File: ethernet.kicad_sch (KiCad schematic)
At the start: 43 parts, among them J5 ARJM11D7-502-AB-EW2, U1 MIMX8MM6DVTLZAA, U23 RTL8211FD, U24 TPD4EUSB30, U25 TPD4EUSB30, Y2 25MHz

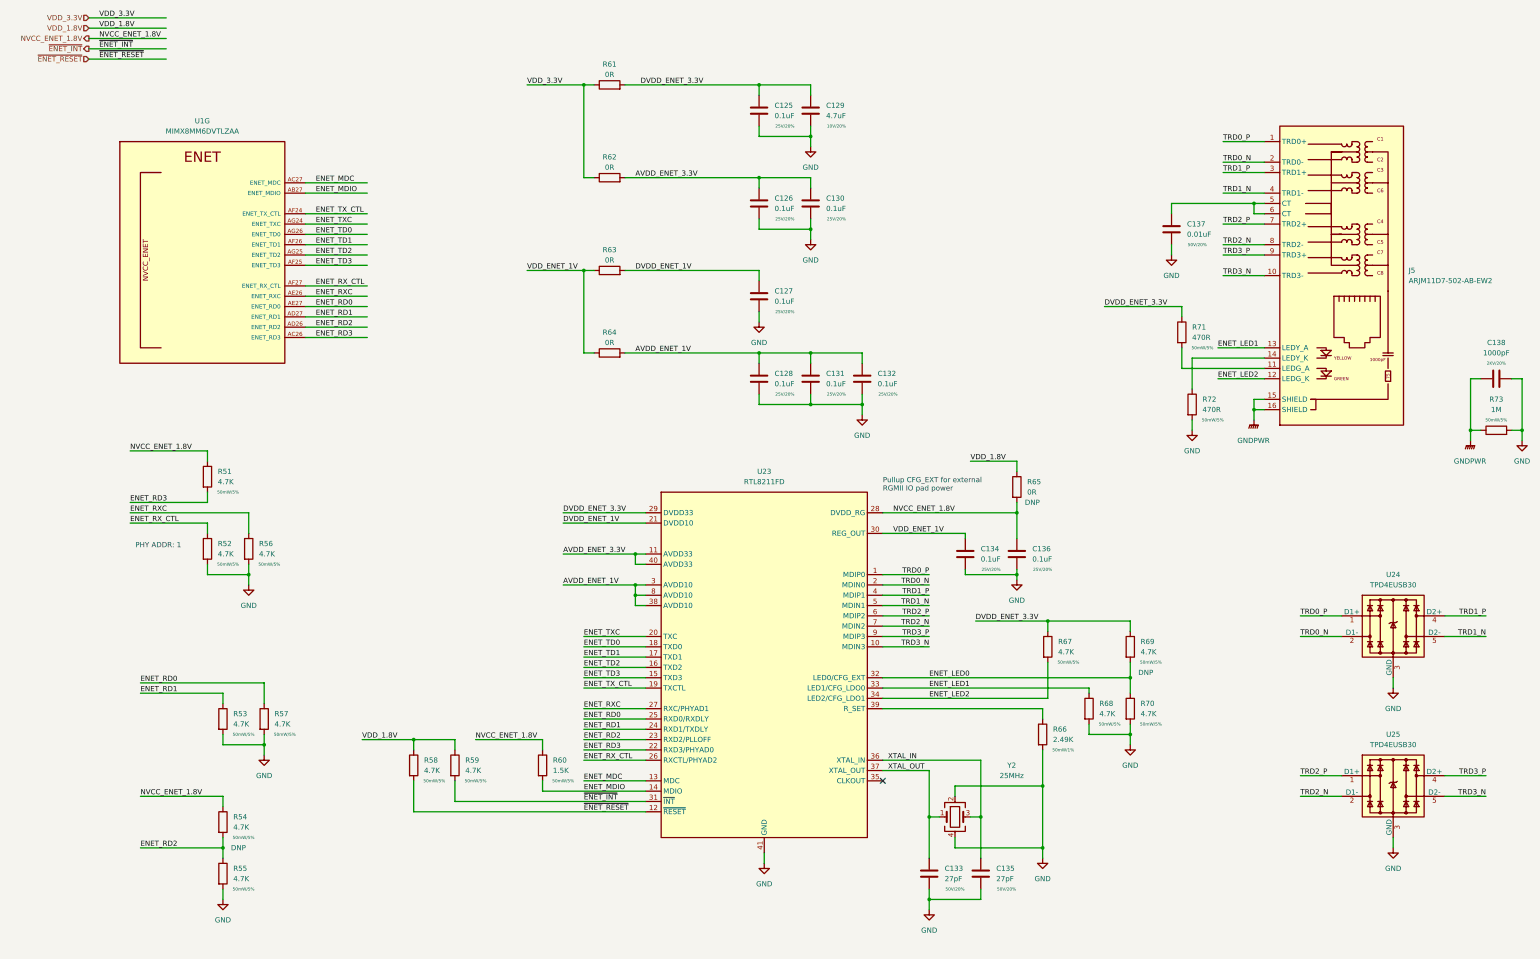
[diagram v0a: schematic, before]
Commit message: add inital ddr tool version, lots of routing work
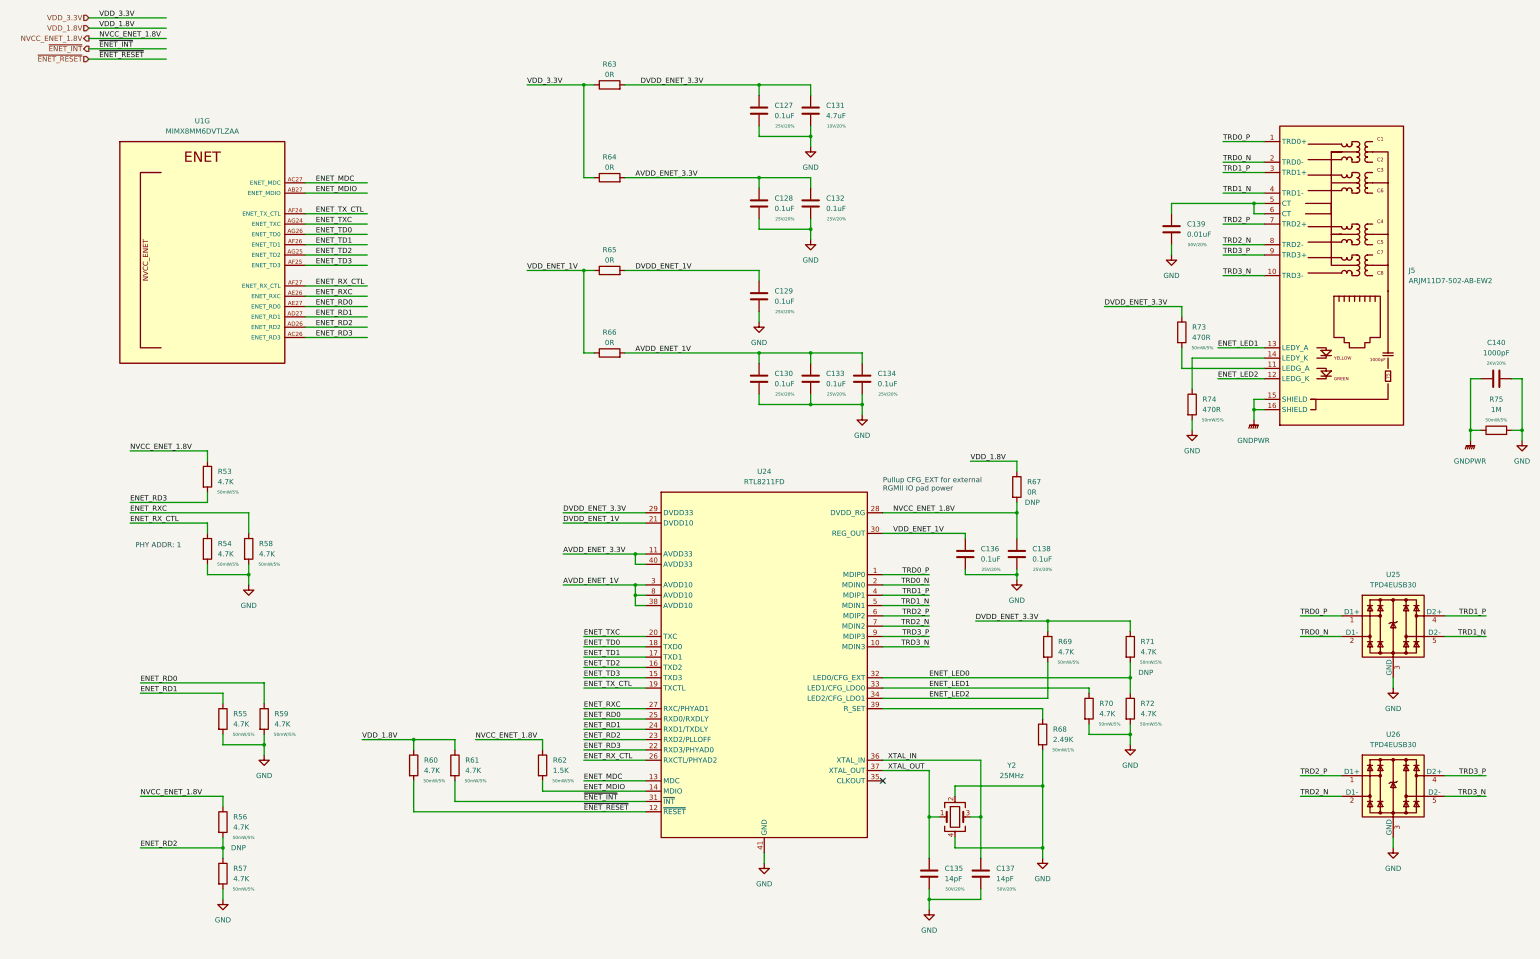
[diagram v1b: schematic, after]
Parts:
- C135: renamed from C133; value 27pF -> 14pF
- C137: renamed from C135; value 27pF -> 14pF
- Y2: MPN (none) -> ECS-250-10-33B-CWN-TR
- renumbered C125 to C127, C126 to C128, C127 to C129, C128 to C130, C129 to C131, C130 to C132, C131 to C133, C132 to C134, C134 to C136, C136 to C138, C137 to C139, C138 to C140, R51 to R53, R52 to R54, R53 to R55, R54 to R56, R55 to R57, R56 to R58, R57 to R59, R58 to R60, R59 to R61, R60 to R62, R61 to R63, R62 to R64, R63 to R65, R64 to R66, R65 to R67, R66 to R68, R67 to R69, R68 to R70, R69 to R71, R70 to R72, R71 to R73, R72 to R74, R73 to R75, U23 to U24, U24 to U25, U25 to U26

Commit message: v2 of ddr flytimes tool, lots of routing work, sch fixes
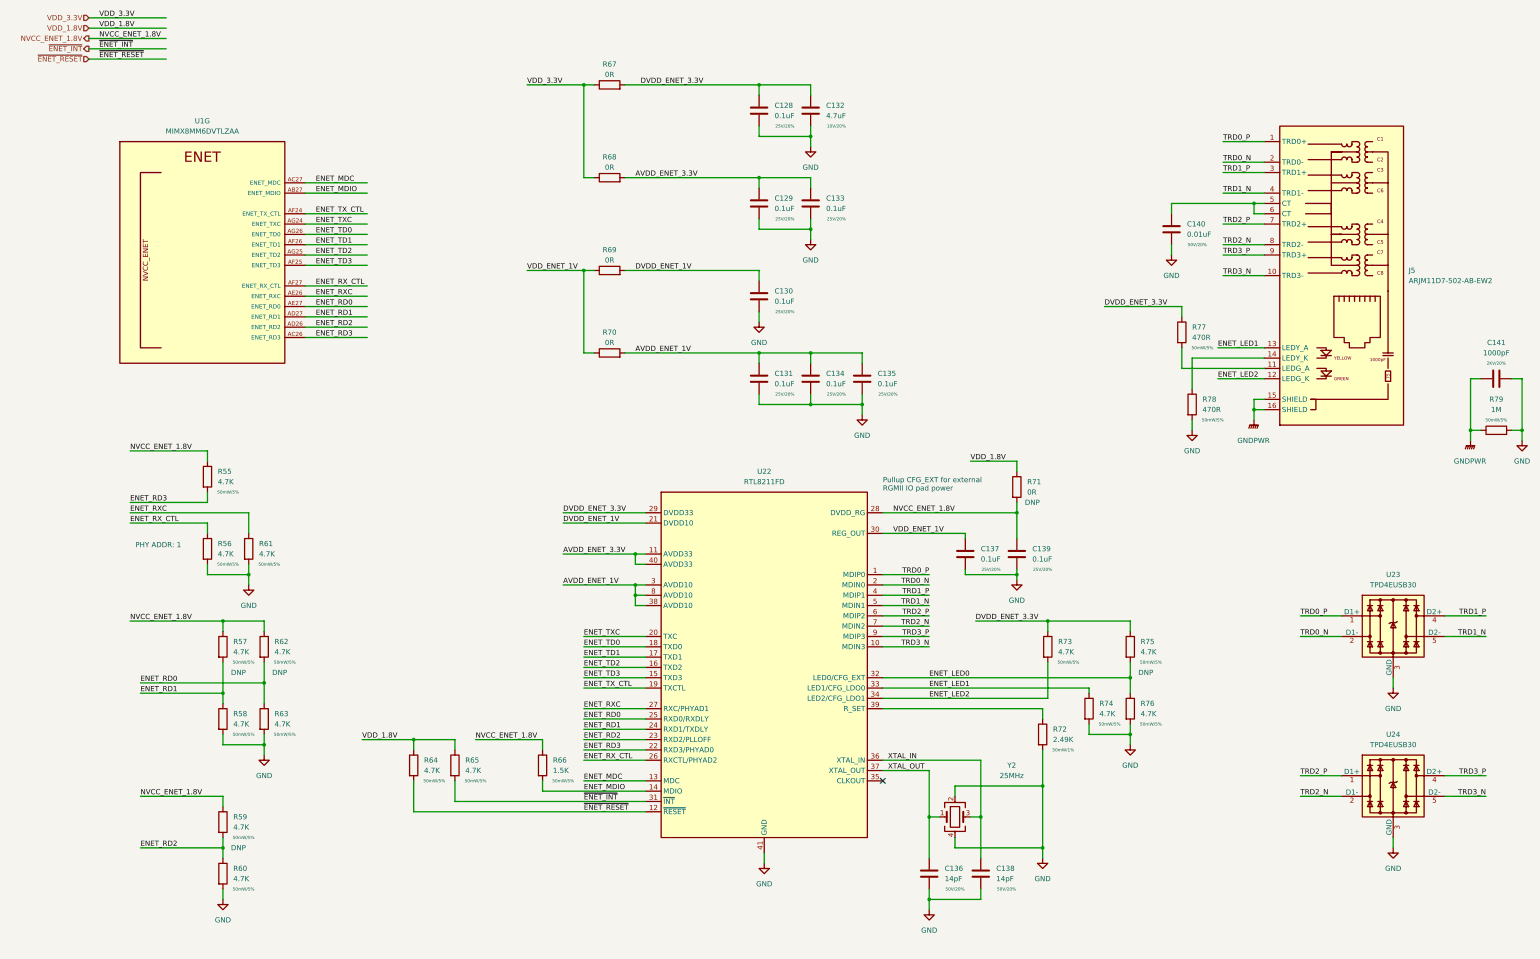
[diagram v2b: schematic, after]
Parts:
- added R57, R62: 4.7K, Resistor_SMD:R_0402_1005Metric, symbol Device:R
- renumbered C127 to C128, C128 to C129, C129 to C130, C130 to C131, C131 to C132, C132 to C133, C133 to C134, C134 to C135, C135 to C136, C136 to C137, C137 to C138, C138 to C139, C139 to C140, C140 to C141, R53 to R55, R54 to R56, R55 to R58, R56 to R59, R57 to R60, R58 to R61, R59 to R63, R60 to R64, R61 to R65, R62 to R66, R63 to R67, R64 to R68, R65 to R69, R66 to R70, R67 to R71, R68 to R72, R69 to R73, R70 to R74, R71 to R75, R72 to R76, R73 to R77, R74 to R78, R75 to R79, U24 to U22, U25 to U23, U26 to U24
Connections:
- net ENET_RD0: now also R62.2
- net ENET_RD1: now also R57.2
- net NVCC_ENET_1.8V: now also R57.1, R62.1

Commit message: more routing work, prepare to change to x32 lpddr4
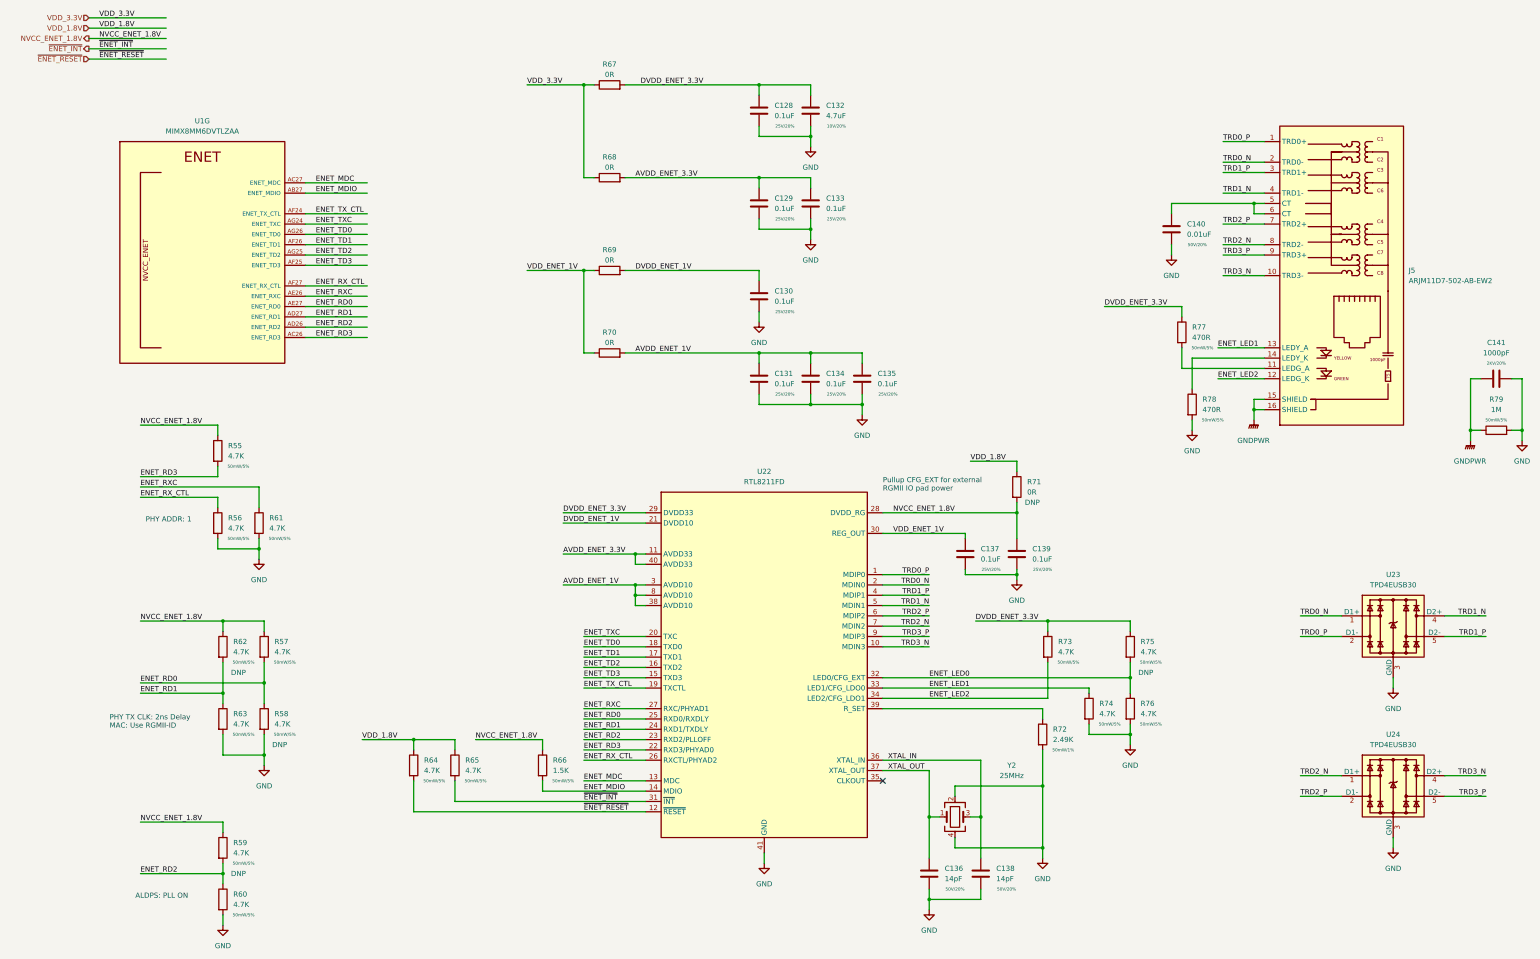
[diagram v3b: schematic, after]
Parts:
- R57: DNP DNP -> (none)
- R58: DNP (none) -> DNP
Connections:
- net ENET_RD0: now also R57.2, R58.1; no longer R62.2, R63.1
- net ENET_RD1: now also R62.2, R63.1; no longer R57.2, R58.1
- net TRD0_N: now also U23.1 (D1+), U23.10; no longer U23.2 (D1-), U23.9
- net TRD0_P: now also U23.2 (D1-), U23.9; no longer U23.1 (D1+), U23.10
- net TRD1_N: now also U23.4 (D2+), U23.7; no longer U23.5 (D2-), U23.6
- net TRD1_P: now also U23.5 (D2-), U23.6; no longer U23.4 (D2+), U23.7
- net TRD2_N: now also U24.1 (D1+), U24.10; no longer U24.2 (D1-), U24.9
- net TRD2_P: now also U24.2 (D1-), U24.9; no longer U24.1 (D1+), U24.10
- net TRD3_N: now also U24.4 (D2+), U24.7; no longer U24.5 (D2-), U24.6
- net TRD3_P: now also U24.5 (D2-), U24.6; no longer U24.4 (D2+), U24.7
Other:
- note added: "ALDPS: PLL ON"
- note added: "PHY TX CLK: 2ns Delay MAC: Use RGMII-ID"
- moved on the sheet: R55, R56, R57, R58, R59, R60, R61, R62, R63

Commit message: inital routing of ddr data bus, sch work
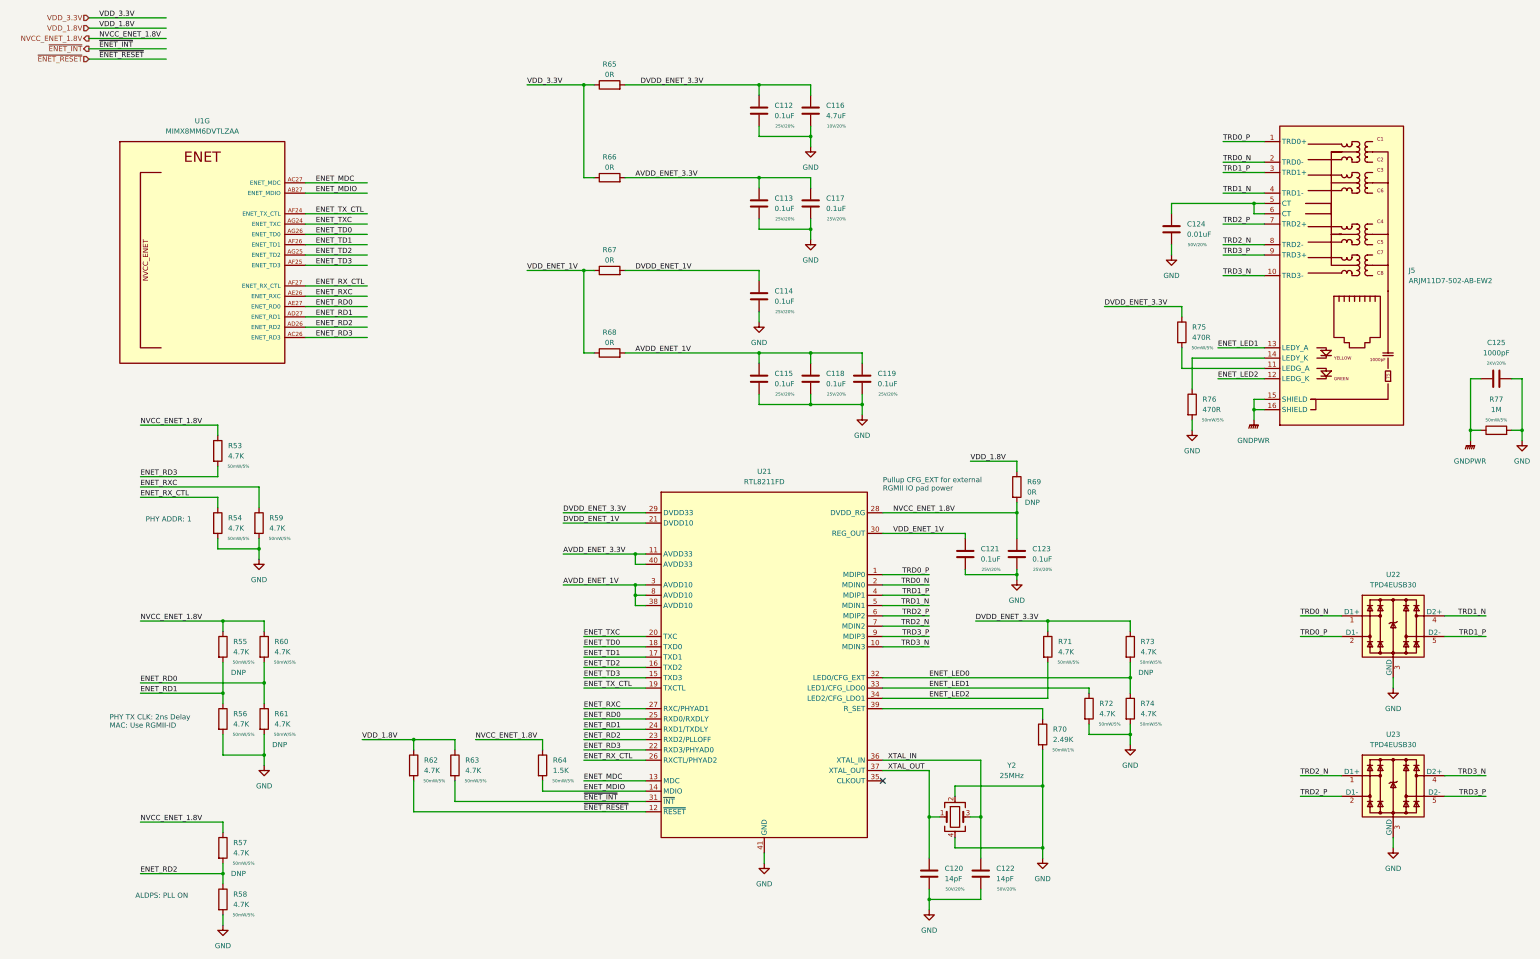
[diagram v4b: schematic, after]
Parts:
- renumbered C128 to C112, C129 to C113, C130 to C114, C131 to C115, C132 to C116, C133 to C117, C134 to C118, C135 to C119, C136 to C120, C137 to C121, C138 to C122, C139 to C123, C140 to C124, C141 to C125, R55 to R53, R56 to R54, R62 to R55, R63 to R56, R59 to R57, R60 to R58, R61 to R59, R57 to R60, R58 to R61, R64 to R62, R65 to R63, R66 to R64, R67 to R65, R68 to R66, R69 to R67, R70 to R68, R71 to R69, R72 to R70, R73 to R71, R74 to R72, R75 to R73, R76 to R74, R77 to R75, R78 to R76, R79 to R77, U22 to U21, U23 to U22, U24 to U23

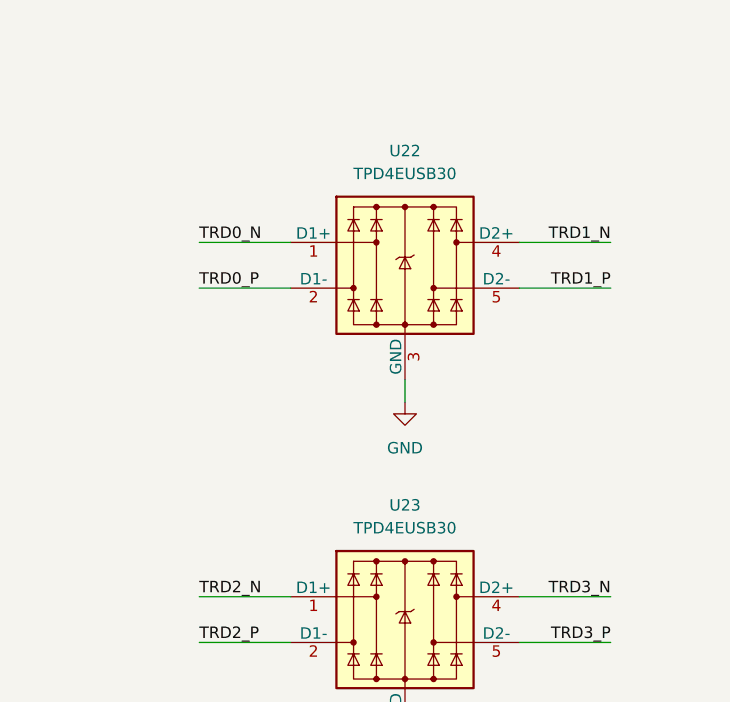
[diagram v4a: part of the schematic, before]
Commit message: add SN65DSI86 DSI2DP ic, SCH, PCB work, flytime work
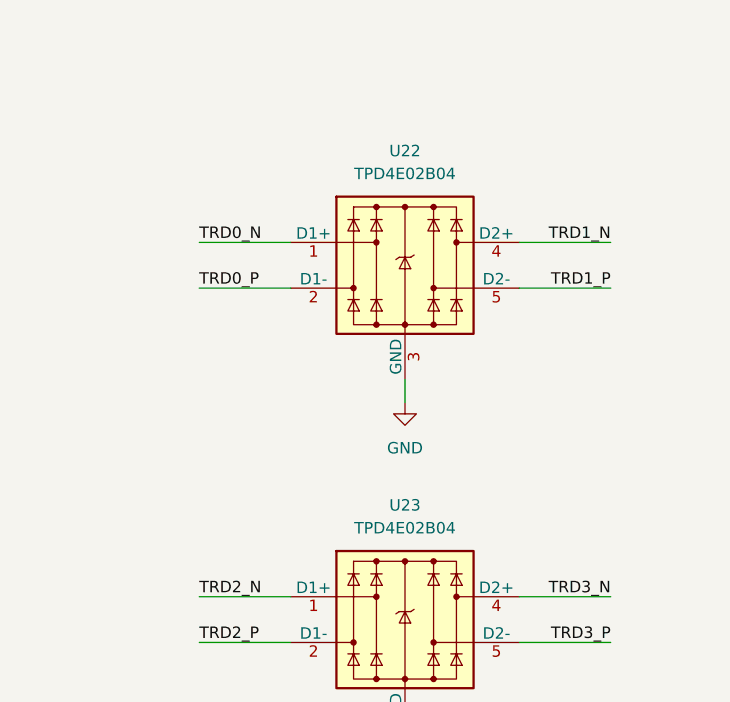
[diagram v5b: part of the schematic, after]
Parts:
- removed U22, U23: TPD4EUSB30, Package_SON:USON-10_2.5x1.0mm_P0.5mm, symbol qsbc:TPD4EUSB30
- added U22, U23: TPD4E02B04, Package_SON:USON-10_2.5x1.0mm_P0.5mm, symbol qsbc:TPD4E02B04
- R53, R54, R55, R56, R57, R58, R59, R60, R61: footprint Resistor_SMD:R_0402_1005Metric -> qsbc:R_0201_0603Metric
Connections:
- net GND: now also U22.3 (GND), U22.8 (GND), U23.3 (GND), U23.8 (GND)
- net TRD0_N: now also U22.1 (D1+), U22.10
- net TRD0_P: now also U22.2 (D1-), U22.9
- net TRD1_N: now also U22.4 (D2+), U22.7
- net TRD1_P: now also U22.5 (D2-), U22.6
- net TRD2_N: now also U23.1 (D1+), U23.10
- net TRD2_P: now also U23.2 (D1-), U23.9
- net TRD3_N: now also U23.4 (D2+), U23.7
- net TRD3_P: now also U23.5 (D2-), U23.6
